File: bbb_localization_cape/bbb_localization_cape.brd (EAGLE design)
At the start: 71.8 x 54.6 mm, 31 parts, among them J2 MOLEX-22-03-5035, U1 SN65HVD256DR, U2 ARDUCAMOV5642, U3 SN74LV1T126DCKR, U4 MSP430G2553IPW20R, U5 SN74LV1T125DCKR, U6 LP38693MP-3.3/NOPB, U7 LM1085ISX-ADJ, U8 SN74LV1T126DCKR

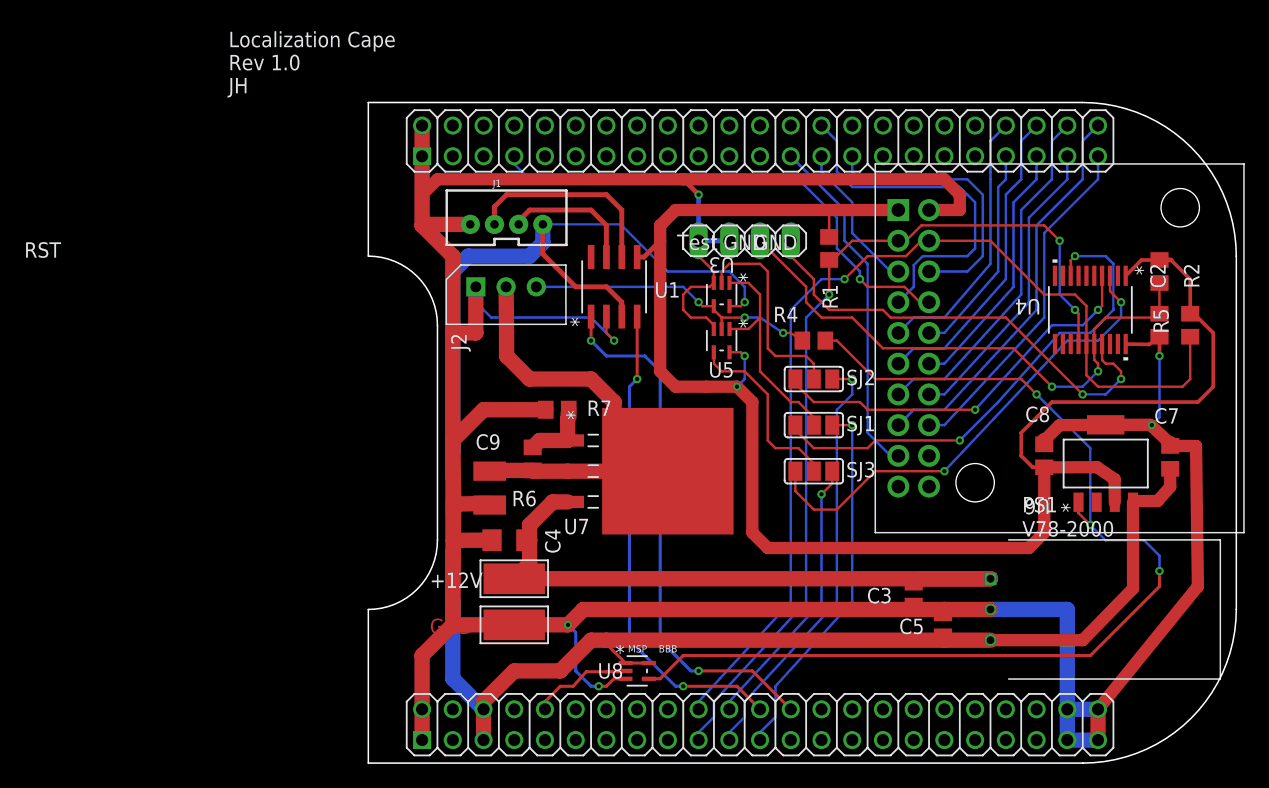
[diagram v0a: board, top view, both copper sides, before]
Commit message: Finished routing signals, passing ERC and DRC
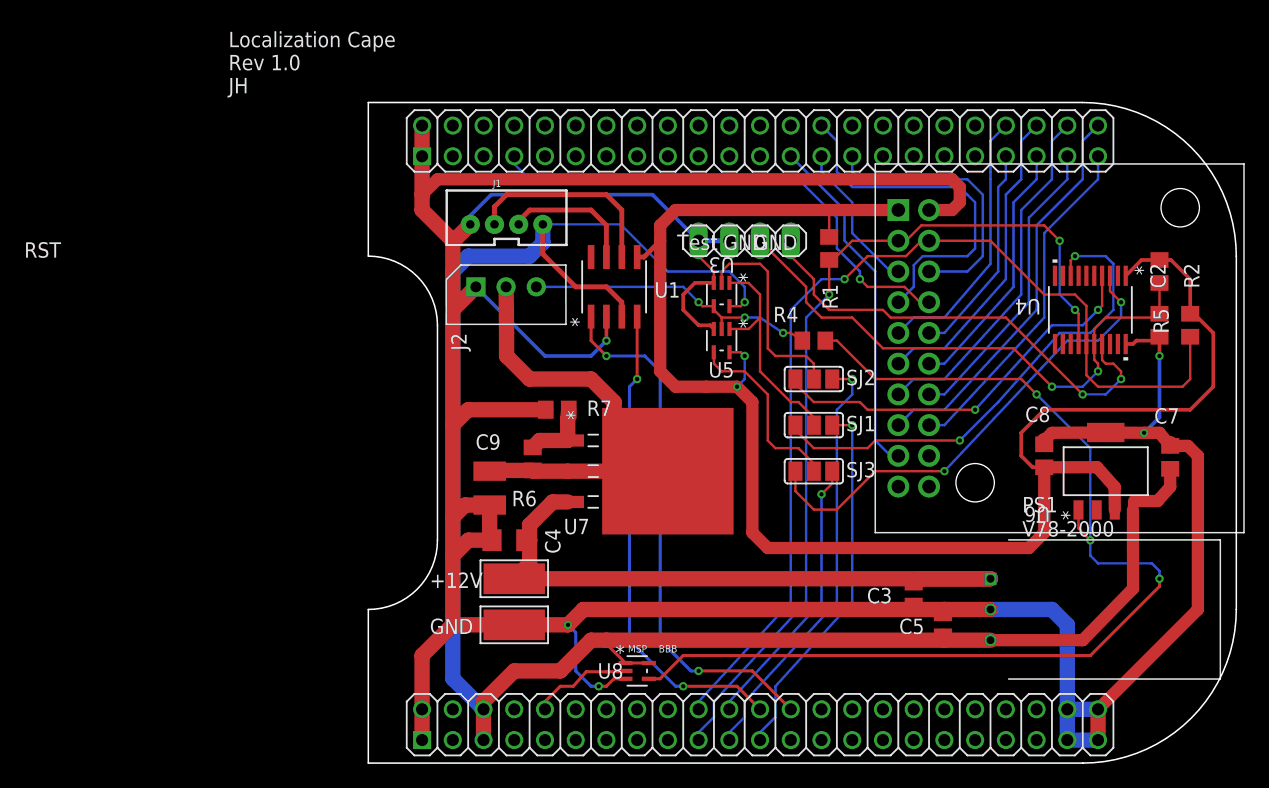
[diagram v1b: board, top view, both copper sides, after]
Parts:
- moved U6 0.64 mm to (75.6, 24.1)
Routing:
- net GND: track 294.4 -> 305.7 mm, vias 6 -> 5
- net SYS_RESETN_5V: track 88.9 -> 90.3 mm

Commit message: Labeled everything
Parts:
- removed C8: 4.7uF, resistor:C0805
- removed R7: 910, resistor:R0805
- added C1: 100nF, resistor:C0805
- added R3: 10k, resistor:R0805
- C2: value 100nF -> 10uF; device resistor:C0805 -> resistor:C1206
- C4: value 10uF -> 22uF; device resistor:C1206 -> resistor:C0805
- C5: value 22uF -> 1uF
- C7: value 1uF -> 4.7uF
- R4: value 10k -> 47k
- R5: value 47k -> 130
- R6: value 130 -> 910
- U3: value SN74LV1T126DCKR -> MSP430G2553IPW20R; device bbb_localization_cape:DCK5 -> bbb_cape_parts:PW20
- U4: value MSP430G2553IPW20R -> SN74LV1T126DCKR; device bbb_cape_parts:PW20 -> bbb_localization_cape:DCK5
- U6: value LP38693MP-3.3/NOPB -> SN74LV1T126DCKR; device bbb_localization_cape:MP05A -> bbb_localization_cape:DCK5
- U7: value LM1085ISX-ADJ -> LP38693MP-3.3/NOPB; device bbb_localization_cape:TS3B -> bbb_localization_cape:MP05A
- U8: value SN74LV1T126DCKR -> LM1085ISX-ADJ; device bbb_localization_cape:DCK5 -> bbb_localization_cape:TS3B
- moved C2 56.6 mm to (26.2, 18.4), turned to 180 degrees
- moved R5 54.1 mm to (28.2, 25.1), turned to 270 degrees
- moved U6 42.1 mm to (36.8, 7.62), turned to 0 degrees
- moved C4 36.6 mm to (62.1, 11.4), turned to 90 degrees
- moved U7 36.2 mm to (75.6, 24.1), turned to 90 degrees
- moved U3 30.5 mm to (74.3, 37.5)
- moved U4 30.5 mm to (43.8, 38.7)
- moved R4 29.1 mm to (80.0, 40.6), turned to 90 degrees
- moved C5 23.3 mm to (80.9, 25.3)
- moved U8 16.7 mm to (39.4, 24.1), turned to 270 degrees
- moved C7 10.4 mm to (70.5, 25.4)
- moved R6 4.54 mm to (30.2, 29.2), turned to 0 degrees
- moved SJ1 3.81 mm to (51.4, 31.8)
- moved SJ2 3.81 mm to (51.4, 27.9)
- renumbered +12V to PAD1, C9 to C6, GND to PAD2
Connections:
- net +10V: now also R5.2, U8.2, U8.4; no longer R6.2, U7.2, U7.4
- net +12V: now also C2.1, U8.3; no longer C4.1, U7.3
- net +3V3: now also C7.1, R4.2, U3.1, U7.3; no longer C8.1, R5.2, U4.1, U6.3
- net +5V: now also C4.1, U4.5, U6.1, U6.5, U7.4; no longer C7.1, U3.5, U6.4, U8.1, U8.5
- net DATA_DYN: now also R3.1, U4.4; no longer R4.1, U3.4
- net GND: now also C1.2, R6.1, U3.20, U4.3, U6.3, U7.5; no longer C8.2, R7.1, U3.3, U4.20, U6.5, U8.3
- net I2C2_SCL: now also U3.14; no longer U4.14
- net I2C2_SDA: now also U3.15; no longer U4.15
- net N$3: now also R5.1, R6.2, U8.1; no longer R6.1, R7.2, U7.1
- net RST: now also C1.1, R4.1, U3.16; no longer C2.1, R5.1, U4.16
- net SYS_RESETN: now also U6.2; no longer U8.2
- net SYS_RESETN_5V: now also R3.2, U6.4, U7.1; no longer R4.2, U6.1, U8.4
- net TEST: now also U3.17; no longer U4.17
- net UART2_DIR: now also SJ2.3; no longer SJ1.3
- net UART2_TXD: now also SJ1.3; no longer SJ2.3
- net UART_DYN_DIR: now also SJ2.2, U4.1; no longer SJ1.2, U3.1
- net UART_DYN_TXD: now also SJ1.2, U4.2; no longer SJ2.2, U3.2
- net UART_MSP_DIR: now also SJ2.1, U3.8; no longer SJ1.1, U4.8
- net UART_MSP_RXD: now also U3.3; no longer U4.3
- net UART_MSP_TXD: now also SJ1.1, U3.4; no longer SJ2.1, U4.4
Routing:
- net UART_MSP_RXD: track 39.8 -> 42.0 mm
- net I2C2_SDA: track 83.5 -> 84.0 mm
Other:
- board text added: "SD1714 Localization Device Cape Jacob Huesman 10/10/2017 Rev. 1.0"
- board text removed: "Localization Cape Rev 1.0 JH"

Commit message: Done, needs external review
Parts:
- C2: device resistor:C1206 -> resistor:C0805
- moved R6 1.02 mm to (29.2, 29.2)
- moved R5 0.36 mm to (27.9, 25.4)
- moved C5 0.28 mm to (80.6, 25.4)
- moved C2 0.19 mm to (26.0, 18.4)
- moved C6 0.18 mm to (24.8, 22.9)
- moved C4 0.13 mm to (62.2, 11.4)
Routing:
- net SYS_RESETN_5V: track 90.3 -> 84.5 mm
- net N$3: track 5.68 -> 6.42 mm
- net GND: track 305.7 -> 306.4 mm
- net +12V: track 55.0 -> 55.7 mm
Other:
- board text added: "12V"
- board text added: "J1"
- board text added: "JP1"
- board text added: "SD1714 Localization Device Cape 10/10/2017 Rev. 1.0 Jacob Huesman"
- board text added: "SJ1"
- board text added: "SJ2"
- board text added: "SJ3"
- board text added: "TST"
- board text removed: "SD1714 Localization Device Cape Jacob Huesman 10/10/2017 Rev. 1.0"
- board text removed: "Test"

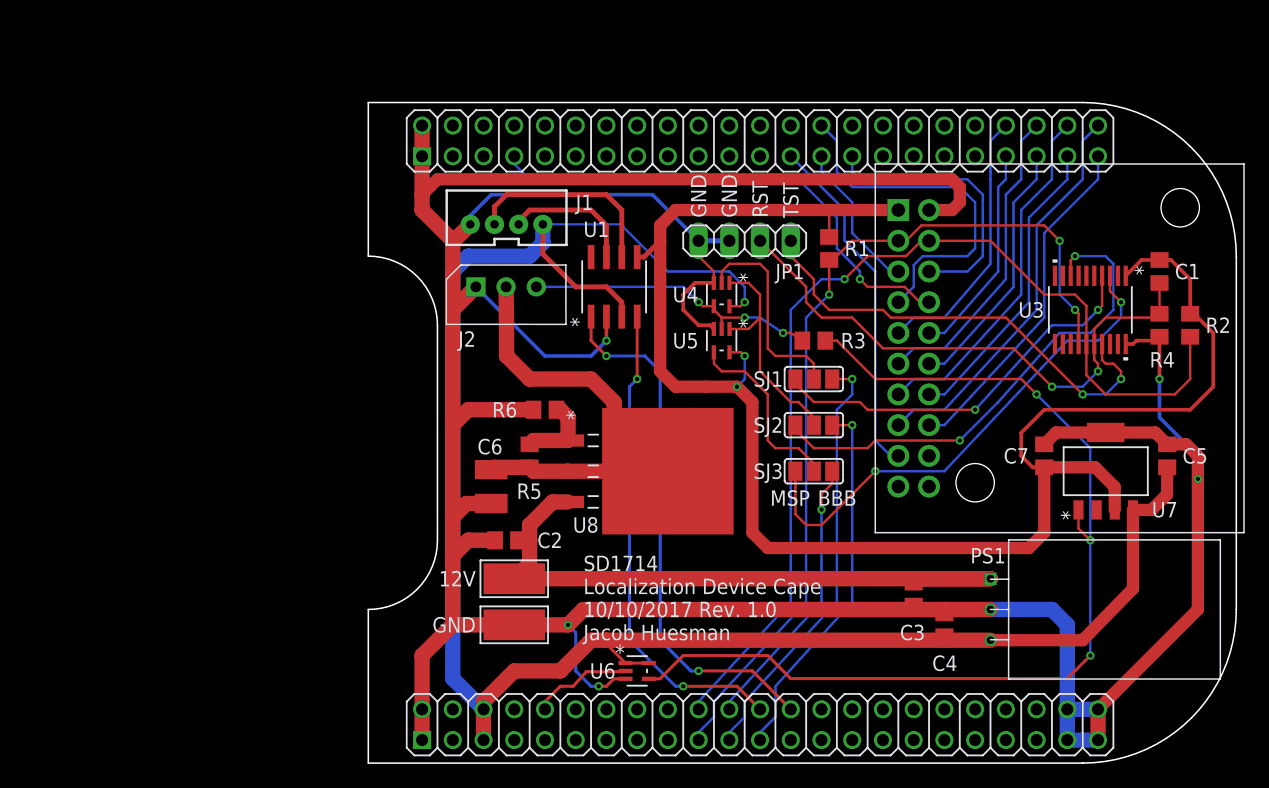
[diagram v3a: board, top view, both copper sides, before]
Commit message: Added ground plane
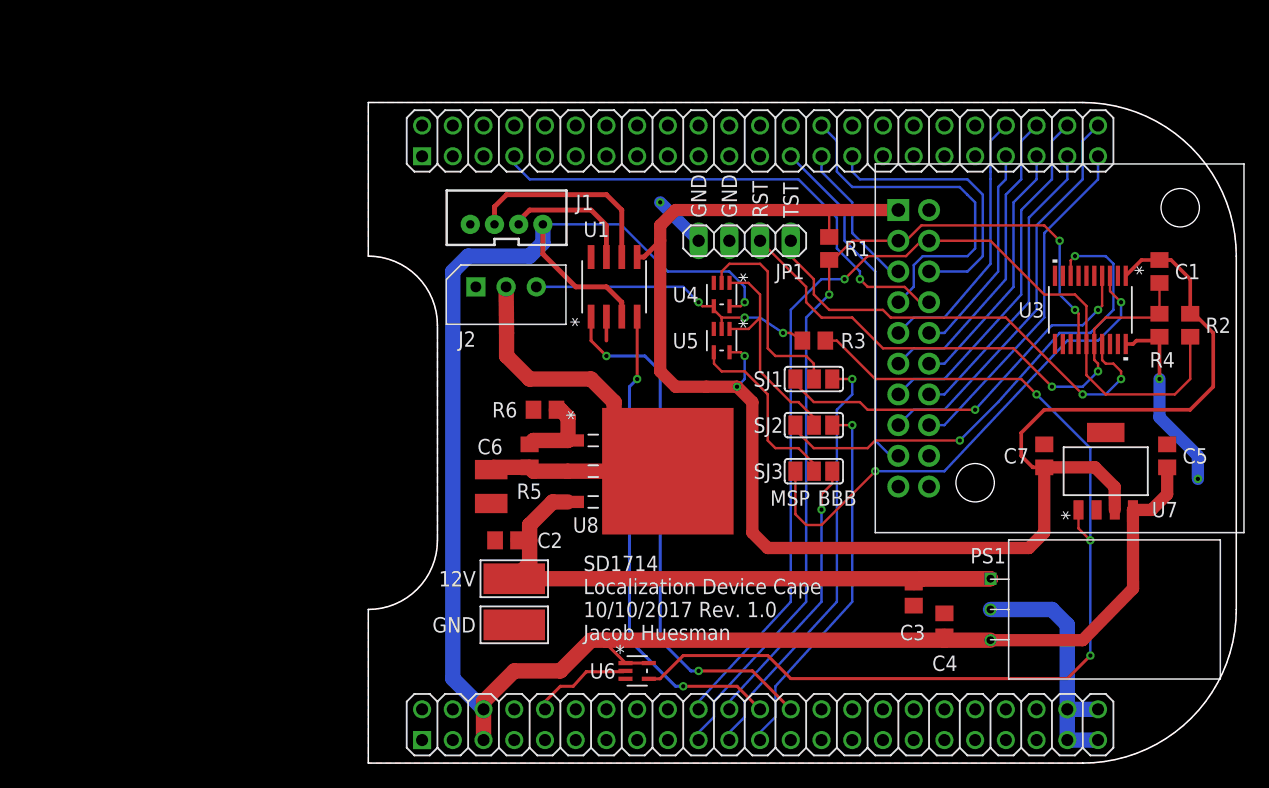
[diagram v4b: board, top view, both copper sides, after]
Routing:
- net GND: track 306.4 -> 44.1 mm, vias 5 -> 3
- added copper zone on layer 1, net GND
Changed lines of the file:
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@@
 <contactref element="A1" pad="92"/>
 <contactref element="U6" pad="3"/>
-<wire x1="19.05" y1="1.905" x2="19.05" y2="4.445" width="1.27" layer="1"/>
 <wire x1="66.04" y1="12.7" x2="71.12" y2="12.7" width="1.27" layer="16"/>
 <wire x1="71.12" y1="12.7" x2="72.39" y2="11.43" width="1.27" layer="16"/>
@@
 <wire x1="72.39" y1="4.445" x2="72.39" y2="1.905" width="1.27" layer="16"/>
 <wire x1="72.39" y1="1.905" x2="74.93" y2="1.905" width="1.27" layer="16"/>
-<wire x1="74.93" y1="1.905" x2="74.93" y2="4.445" width="1.27" layer="1"/>
 <wire x1="74.93" y1="4.445" x2="72.39" y2="4.445" width="1.27" layer="16"/>
-<wire x1="74.93" y1="4.445" x2="83.185" y2="12.7" width="1.016" layer="1"/>
-<wire x1="83.185" y1="23.495" x2="83.185" y2="12.7" width="1.016" layer="1"/>
-<wire x1="19.05" y1="52.705" x2="19.05" y2="50.165" width="1.27" layer="1"/>
-<wire x1="41.91" y1="43.18" x2="44.45" y2="43.18" width="0.4064" layer="16"/>
-<wire x1="35.8648" y1="6.97" x2="34.91" y2="6.97" width="0.254" layer="1"/>
-<wire x1="34.91" y1="6.97" x2="34.29" y2="6.35" width="0.254" layer="1"/>
-<wire x1="34.29" y1="6.35" x2="33.655" y2="6.35" width="0.254" layer="1"/>
-<via x="33.655" y="6.35" extent="1-16" drill="0.35"/>
-<wire x1="33.655" y1="6.35" x2="33.02" y2="6.35" width="0.254" layer="16"/>
-<wire x1="33.02" y1="6.35" x2="31.75" y2="7.62" width="0.254" layer="16"/>
-<wire x1="31.75" y1="7.62" x2="31.75" y2="10.795" width="0.254" layer="16"/>
-<wire x1="31.75" y1="10.795" x2="31.115" y2="11.43" width="0.254" layer="16"/>
-<via x="31.115" y="11.43" extent="1-16" drill="0.35"/>
-<wire x1="62.23" y1="12.7" x2="66.04" y2="12.7" width="1.27" layer="1"/>
-<wire x1="59.69" y1="12.7" x2="62.23" y2="12.7" width="1.27" layer="1"/>
-<wire x1="59.69" y1="12.7" x2="32.385" y2="12.7" width="1.27" layer="1"/>
-<wire x1="32.385" y1="12.7" x2="31.115" y2="11.43" width="1.27" layer="1"/>
-<wire x1="26.67" y1="11.43" x2="31.115" y2="11.43" width="1.27" layer="1"/>
-<wire x1="62.23" y1="12.38" x2="62.103" y2="12.573" width="1.27" layer="1"/>
-<wire x1="62.103" y1="12.573" x2="62.23" y2="12.7" width="1.27" layer="1"/>
-<wire x1="59.69" y1="13.02" x2="59.69" y2="12.7" width="1.27" layer="1"/>
-<wire x1="43.165" y1="40.625" x2="43.165" y2="39.7002" width="0.2032" layer="1"/>
-<wire x1="43.165" y1="40.625" x2="43.18" y2="40.64" width="0.2032" layer="1"/>
-<wire x1="43.18" y1="40.64" x2="41.925" y2="41.895" width="0.2032" layer="1"/>
-<wire x1="41.925" y1="41.895" x2="41.91" y2="43.18" width="0.2032" layer="1"/>
 <wire x1="80.01" y1="35.245" x2="80.01" y2="31.75" width="0.3048" layer="1"/>
 <via x="80.01" y="31.75" extent="1-16" drill="0.35"/>
-<wire x1="19.05" y1="4.445" x2="19.05" y2="8.89" width="1.27" layer="1"/>
-<wire x1="21.59" y1="17.145" x2="21.59" y2="11.43" width="1.27" layer="1"/>
-<wire x1="21.59" y1="20.32" x2="21.59" y2="27.94" width="1.27" layer="1"/>
-<wire x1="21.59" y1="20.32" x2="21.59" y2="17.145" width="1.27" layer="1"/>
-<wire x1="21.59" y1="27.94" x2="21.59" y2="37.465" width="1.27" layer="1"/>
-<wire x1="21.59" y1="37.465" x2="23.495" y2="39.37" width="1.27" layer="1"/>
-<wire x1="21.59" y1="43.18" x2="21.59" y2="37.465" width="1.27" layer="1"/>
-<wire x1="21.59" y1="43.18" x2="21.68" y2="43.18" width="1.27" layer="1"/>
-<wire x1="21.68" y1="43.18" x2="23.035" y2="44.535" width="1.27" layer="1"/>
-<wire x1="19.05" y1="50.165" x2="19.05" y2="46.99" width="1.27" layer="1"/>
-<wire x1="19.05" y1="46.99" x2="19.05" y2="45.72" width="1.27" layer="1"/>
-<wire x1="19.05" y1="45.72" x2="21.59" y2="43.18" width="1.27" layer="1"/>
-<wire x1="25.085" y1="18.415" x2="22.87585" y2="18.43085" width="1.27" layer="1"/>
-<wire x1="22.87585" y1="18.43085" x2="21.59" y2="17.145" width="1.27" layer="1"/>
-<wire x1="28.26" y1="29.21" x2="22.86" y2="29.21" width="1.27" layer="1"/>
-<wire x1="22.86" y1="29.21" x2="21.59" y2="27.94" width="1.27" layer="1"/>
-<wire x1="29.21" y1="33.655" x2="33.02" y2="33.655" width="0.3048" layer="16"/>
-<wire x1="33.02" y1="33.655" x2="34.29" y2="34.925" width="0.3048" layer="16"/>
-<wire x1="23.495" y1="39.37" x2="29.21" y2="33.655" width="0.3048" layer="16"/>
-<via x="34.29" y="34.925" extent="1-16" drill="0.35"/>
 <wire x1="34.29" y1="34.925" x2="34.29" y2="36.9062" width="0.3048" layer="1"/>
-<wire x1="19.05" y1="8.89" x2="21.59" y2="11.43" width="1.27" layer="1"/>
-<wire x1="21.59" y1="11.43" x2="26.67" y2="11.43" width="1.27" layer="1"/>
-<wire x1="43.165" y1="39.7002" x2="41.6052" y2="39.7002" width="0.3048" layer="1"/>
-<wire x1="41.6052" y1="39.7002" x2="40.64" y2="38.735" width="0.3048" layer="1"/>
-<wire x1="40.64" y1="37.465" x2="41.91" y2="36.195" width="0.3048" layer="1"/>
-<wire x1="40.64" y1="38.735" x2="40.64" y2="37.465" width="0.3048" layer="1"/>
-<wire x1="41.91" y1="36.195" x2="42.8602" y2="36.195" width="0.3048" layer="1"/>
-<wire x1="42.8602" y1="36.195" x2="43.165" y2="35.8902" width="0.3048" layer="1"/>
-<wire x1="23.035" y1="44.535" x2="23.035" y2="45.26" width="0.3048" layer="16"/>
-<wire x1="23.035" y1="45.26" x2="24.765" y2="46.99" width="0.3048" layer="16"/>
-<wire x1="24.765" y1="46.99" x2="38.1" y2="46.99" width="0.3048" layer="16"/>
-<wire x1="38.1" y1="46.99" x2="41.91" y2="43.18" width="0.3048" layer="16"/>
-<wire x1="19.05" y1="46.99" x2="20.32" y2="48.26" width="1.016" layer="1"/>
-<wire x1="20.32" y1="48.26" x2="62.865" y2="48.26" width="1.016" layer="1"/>
-<wire x1="62.865" y1="48.26" x2="63.5" y2="47.625" width="1.016" layer="1"/>
-<wire x1="63.5" y1="46.355" x2="62.865" y2="45.72" width="1.016" layer="1"/>
-<wire x1="62.865" y1="45.72" x2="60.96" y2="45.72" width="1.016" layer="1"/>
-<wire x1="63.5" y1="47.625" x2="63.5" y2="46.355" width="1.016" layer="1"/>
 <wire x1="77.219996875" y1="34.6456" x2="77.8256" y2="34.6456" width="0.3048" layer="1"/>
 <wire x1="77.8256" y1="34.6456" x2="78.105" y2="34.925" width="0.3048" layer="1"/>
 <wire x1="78.105" y1="34.925" x2="79.69" y2="34.925" width="0.3048" layer="1"/>
 <wire x1="79.69" y1="34.925" x2="80.01" y2="35.245" width="0.3048" layer="1"/>
-<wire x1="80.01" y1="28.575" x2="80.01" y2="31.75" width="0.3048" layer="16"/>
-<wire x1="80.645" y1="26.35" x2="82.235" y2="26.35" width="1.016" layer="1"/>
-<wire x1="82.235" y1="26.35" x2="83.185" y2="25.4" width="1.016" layer="1"/>
-<wire x1="83.185" y1="25.4" x2="83.185" y2="23.495" width="1.016" layer="1"/>
-<wire x1="24.765" y1="21.46" x2="22.73" y2="21.46" width="1.27" layer="1"/>
-<wire x1="22.73" y1="21.46" x2="21.59" y2="20.32" width="1.27" layer="1"/>
-<wire x1="71.4654" y1="27.3304" x2="75.565" y2="27.3304" width="1.016" layer="1"/>
-<wire x1="71.4654" y1="27.3304" x2="70.485" y2="26.35" width="1.016" layer="1"/>
-<wire x1="75.565" y1="27.3304" x2="79.6646" y2="27.3304" width="1.016" layer="1"/>
-<wire x1="79.6646" y1="27.3304" x2="80.645" y2="26.35" width="1.016" layer="1"/>
+<wire x1="80.01" y1="28.575" x2="80.01" y2="31.75" width="1.016" layer="16"/>
 <via x="83.185" y="23.495" extent="1-16" drill="0.35"/>
-<wire x1="83.185" y1="23.495" x2="83.185" y2="25.4" width="0.3048" layer="16"/>
-<wire x1="83.185" y1="25.4" x2="80.01" y2="28.575" width="0.3048" layer="16"/>
+<wire x1="83.185" y1="23.495" x2="83.185" y2="25.4" width="1.016" layer="16"/>
+<wire x1="83.185" y1="25.4" x2="80.01" y2="28.575" width="1.016" layer="16"/>
+<polygon width="0.1524" layer="1" isolate="0.254">
+<vertex x="14.605" y="54.61"/>
+<vertex x="73.66" y="54.61" curve="-90"/>
+<vertex x="86.36" y="41.91"/>
+<vertex x="86.36" y="12.7" curve="-90"/>
+<vertex x="73.66" y="0"/>
+<vertex x="70.485" y="0"/>
+<vertex x="14.605" y="0"/>
+<vertex x="14.605" y="12.7" curve="90"/>
+<vertex x="20.32" y="18.415"/>
+<vertex x="20.32" y="21.59"/>
+<vertex x="20.32" y="35.56"/>
+<vertex x="20.32" y="36.195" curve="90"/>
+<vertex x="14.605" y="41.91"/>
+</polygon>
+<wire x1="41.91" y1="43.18" x2="38.735" y2="46.355" width="1.016" layer="16"/>
+<via x="38.735" y="46.355" extent="1-16" drill="0.35"/>
 </signal>
 <signal name="+5V">
